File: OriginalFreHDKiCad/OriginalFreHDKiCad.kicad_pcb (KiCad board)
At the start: 2 copper layers, 96.5 x 79 mm, 0 parts

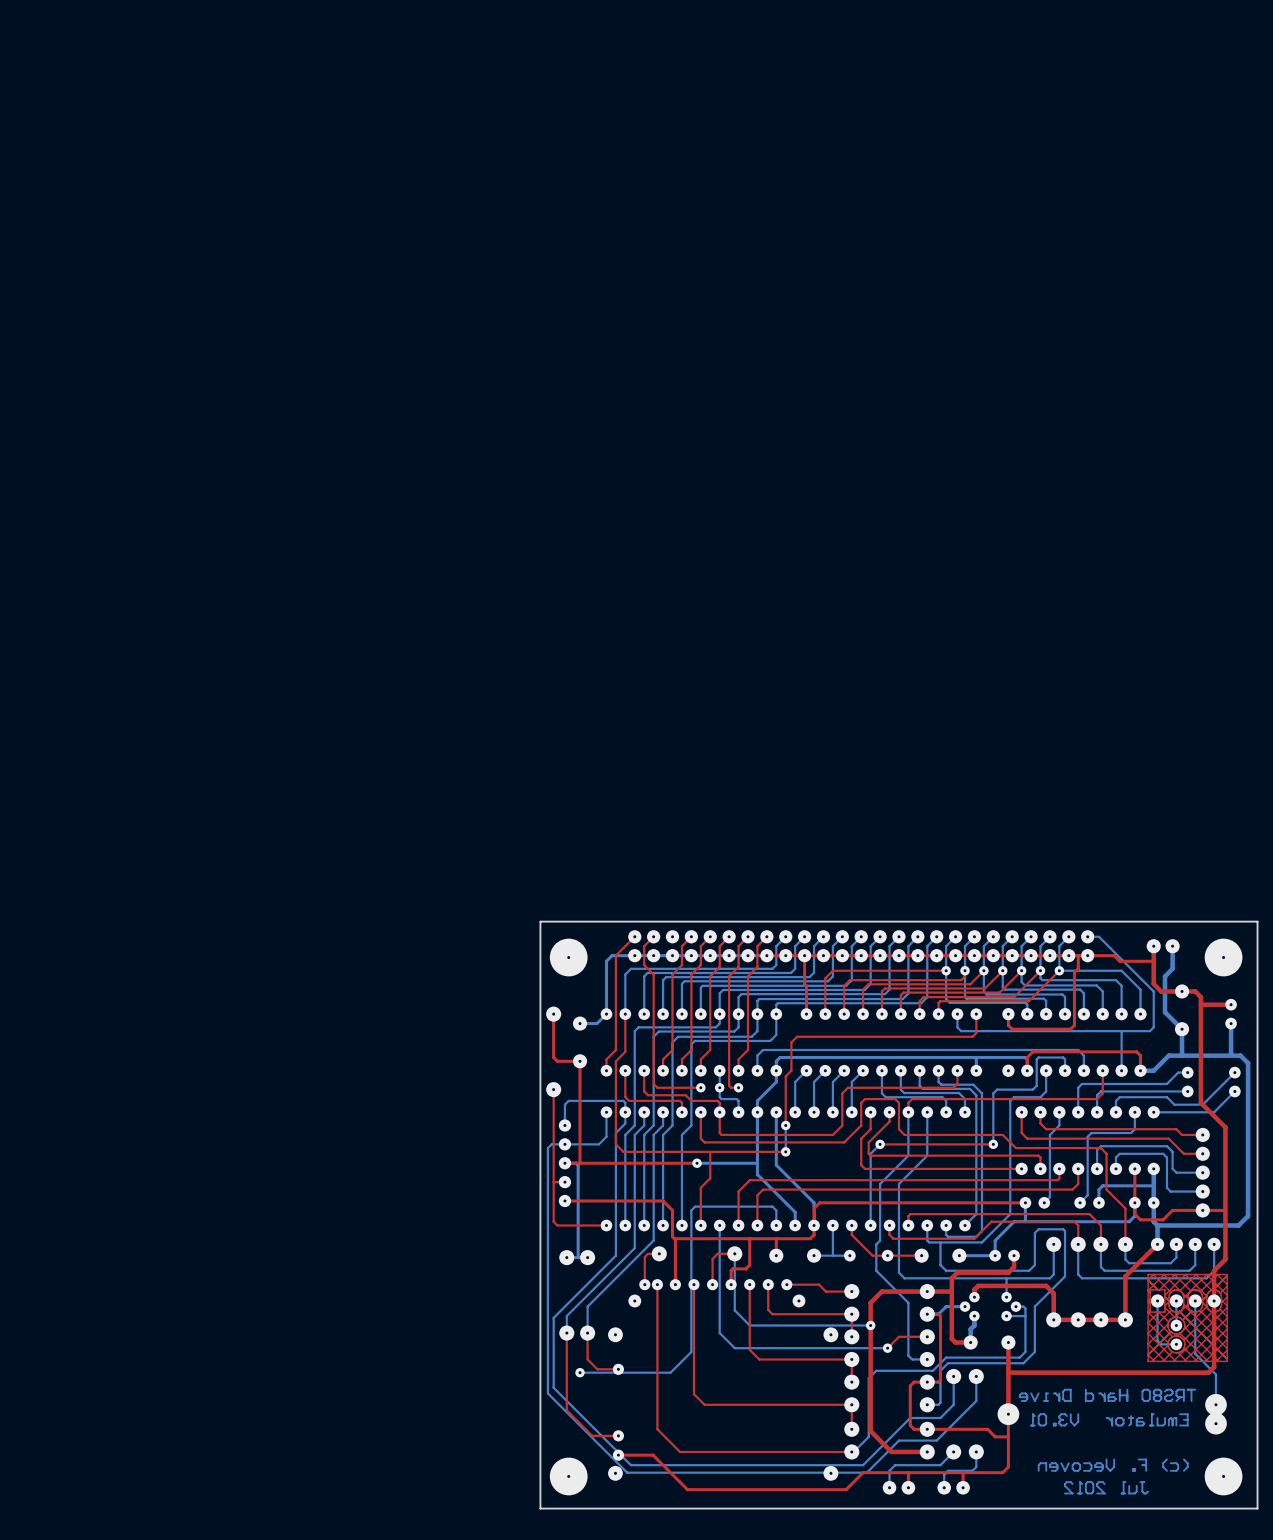
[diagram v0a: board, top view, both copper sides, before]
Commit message: WIP on matching scheamtic to imported gerbers.
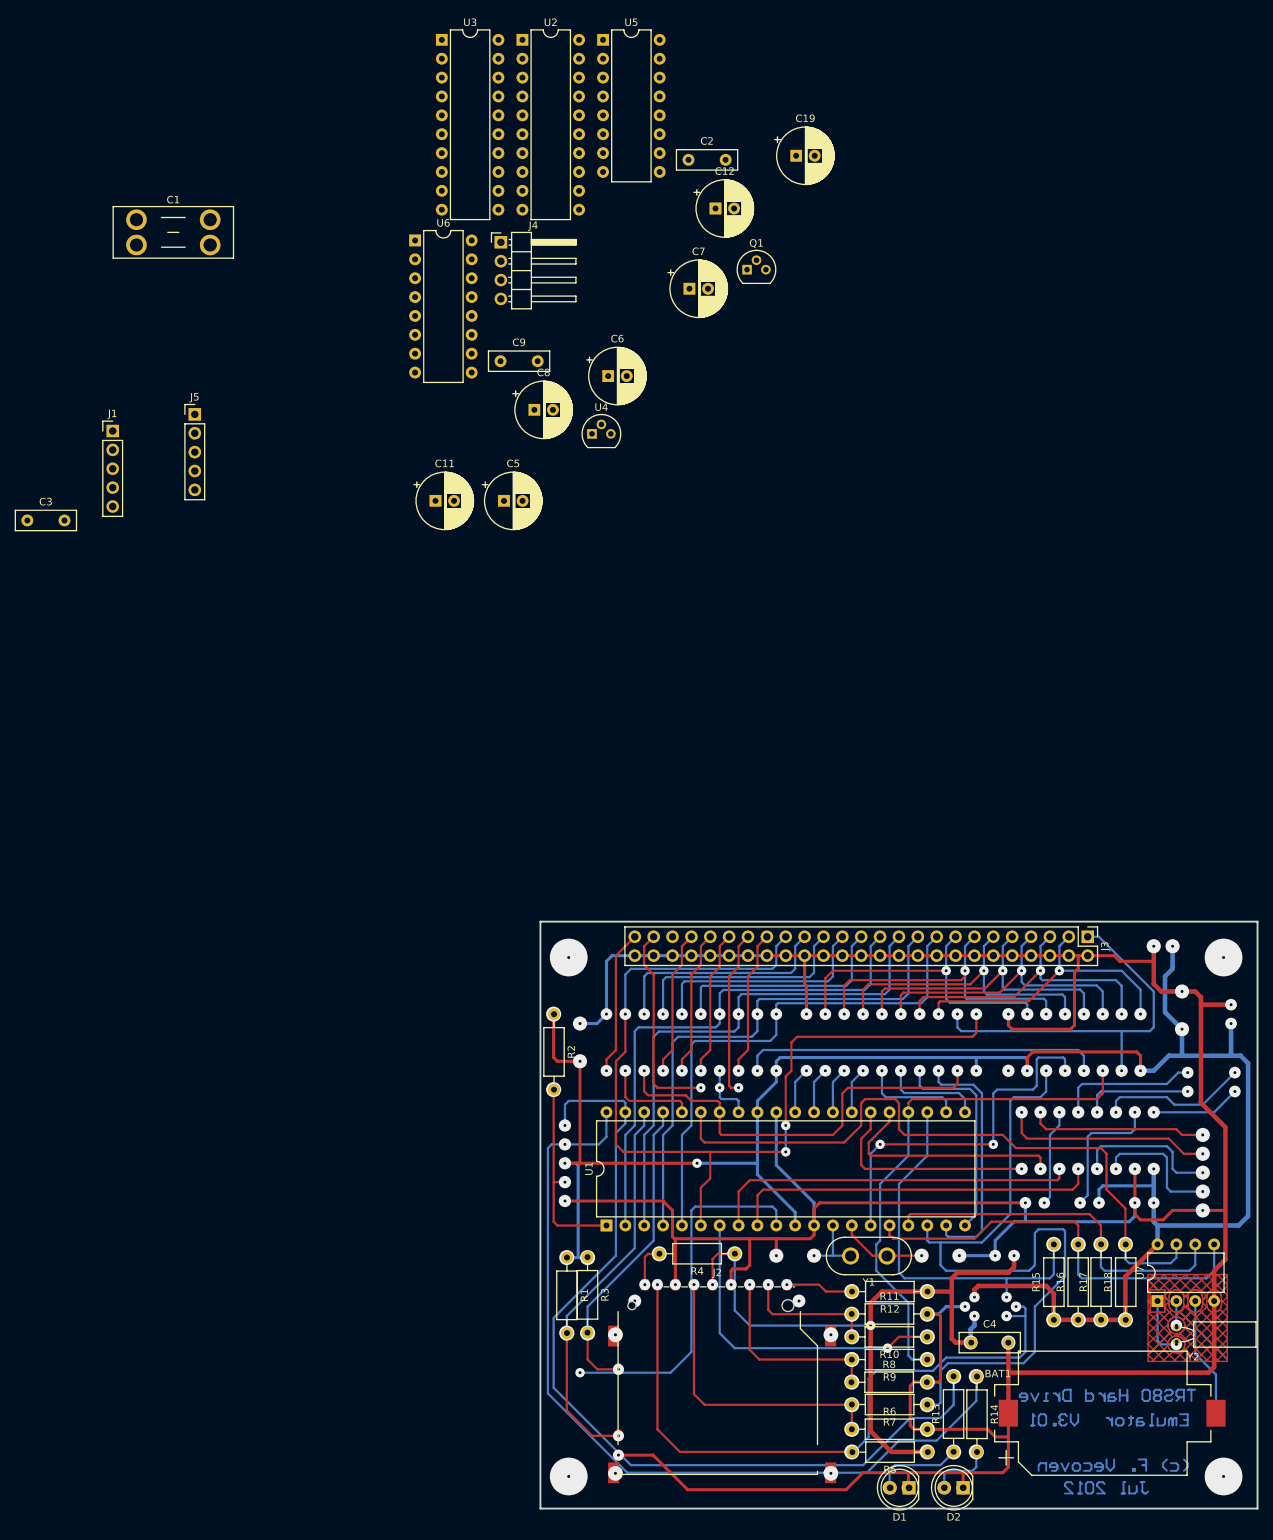
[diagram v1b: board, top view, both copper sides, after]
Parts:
- added BAT1: 3.3V, Battery:BatteryHolder_Keystone_1060_1x2032, F.Cu at (178.7, 123.6)
- added C1: 0.1uF, Fuse:Fuseholder_Blade_Mini_Keystone_3568, F.Cu at (48.6, -37.0)
- added C11: 1uF, Capacitor_THT:CP_Radial_D7.5mm_P2.50mm, F.Cu at (88.9, 0.83)
- added C12: 10uF, Capacitor_THT:CP_Radial_D7.5mm_P2.50mm, F.Cu at (126.6, -38.5)
- added C19: 1uF, Capacitor_THT:CP_Radial_D7.5mm_P2.50mm, F.Cu at (137.4, -45.6)
- added C2: 22pF, Capacitor_THT:C_Disc_D8.0mm_W2.5mm_P5.00mm, F.Cu at (122.9, -45.1)
- added C3: 22pF, Capacitor_THT:C_Disc_D8.0mm_W2.5mm_P5.00mm, F.Cu at (33.9, 3.47)
- added C4: 0.1uF, Capacitor_THT:C_Disc_D8.0mm_W2.5mm_P5.00mm, F.Cu at (161.0, 114.1)
- added C5: 10uF, Capacitor_THT:CP_Radial_D7.5mm_P2.50mm, F.Cu at (98.1, 0.83)
- added C6: 1uF, Capacitor_THT:CP_Radial_D7.5mm_P2.50mm, F.Cu at (112.1, -16.0)
- added C7: 1uF, Capacitor_THT:CP_Radial_D7.5mm_P2.50mm, F.Cu at (123.0, -27.7)
- added C8: 1uF, Capacitor_THT:CP_Radial_D7.5mm_P2.50mm, F.Cu at (102.2, -11.4)
- added C9: 0.1uF, Capacitor_THT:C_Disc_D8.0mm_W2.5mm_P5.00mm, F.Cu at (97.6, -18.0)
- added D1: LED, LED_THT:LED_D5.0mm, F.Cu at (152.6, 133.7)
- added D2: LED, LED_THT:LED_D5.0mm, F.Cu at (159.9, 133.7)
- added J1: CON5, Connector_PinHeader_2.54mm:PinHeader_1x05_P2.54mm_Vertical, F.Cu at (45.4, -8.57)
- added J2: SDCARD, Connector_Card:SD_TE_2041021, F.Cu at (126.8, 118.3)
- added J3: CON50, Connector_PinHeader_2.54mm:PinHeader_2x25_P2.54mm_Vertical, F.Cu at (176.7, 59.5)
- added J4: CON2, Connector_PinHeader_2.54mm:PinHeader_1x04_P2.54mm_Horizontal, F.Cu at (97.7, -34.0)
- added J5: CON5, Connector_PinHeader_2.54mm:PinHeader_1x05_P2.54mm_Vertical, F.Cu at (56.5, -10.8)
- added Q1: BS170, Package_TO_SOT_THT:TO-92, F.Cu at (130.8, -30.3)
- added R1: 1K, Resistor_THT:R_Axial_DIN0207_L6.3mm_D2.5mm_P10.16mm_Horizontal, F.Cu at (106.6, 102.7)
- added R10: 220R, Resistor_THT:R_Axial_DIN0207_L6.3mm_D2.5mm_P10.16mm_Horizontal, F.Cu at (155.0, 113.4)
- added R11: 330R, Resistor_THT:R_Axial_DIN0207_L6.3mm_D2.5mm_P10.16mm_Horizontal, F.Cu at (144.9, 110.3)
- added R12: 10K, Resistor_THT:R_Axial_DIN0207_L6.3mm_D2.5mm_P10.16mm_Horizontal, F.Cu at (155.1, 107.3)
- added R13: 330R, Resistor_THT:R_Axial_DIN0207_L6.3mm_D2.5mm_P10.16mm_Horizontal, F.Cu at (158.6, 128.8)
- added R14: 330R, Resistor_THT:R_Axial_DIN0207_L6.3mm_D2.5mm_P10.16mm_Horizontal, F.Cu at (161.8, 118.7)
- added R15: 10K, Resistor_THT:R_Axial_DIN0207_L6.3mm_D2.5mm_P10.16mm_Horizontal, F.Cu at (172.1, 111.1)
- added R16: 4K7, Resistor_THT:R_Axial_DIN0207_L6.3mm_D2.5mm_P10.16mm_Horizontal, F.Cu at (175.4, 111.1)
- added R17: 4K7, Resistor_THT:R_Axial_DIN0207_L6.3mm_D2.5mm_P10.16mm_Horizontal, F.Cu at (178.4, 111.0)
- added R18: 4K7, Resistor_THT:R_Axial_DIN0207_L6.3mm_D2.5mm_P10.16mm_Horizontal, F.Cu at (181.8, 111.1)
- added R2: 10K, Resistor_THT:R_Axial_DIN0207_L6.3mm_D2.5mm_P10.16mm_Horizontal, F.Cu at (104.8, 69.9)
- added R3: 1K, Resistor_THT:R_Axial_DIN0207_L6.3mm_D2.5mm_P10.16mm_Horizontal, F.Cu at (109.3, 102.6)
- added R4: 10K, Resistor_THT:R_Axial_DIN0207_L6.3mm_D2.5mm_P10.16mm_Horizontal, F.Cu at (129.2, 102.2)
- added R5: 10K, Resistor_THT:R_Axial_DIN0207_L6.3mm_D2.5mm_P10.16mm_Horizontal, F.Cu at (155.1, 128.9)
- added R6: 330R, Resistor_THT:R_Axial_DIN0207_L6.3mm_D2.5mm_P10.16mm_Horizontal, F.Cu at (144.9, 125.8)
- added R7: 220R, Resistor_THT:R_Axial_DIN0207_L6.3mm_D2.5mm_P10.16mm_Horizontal, F.Cu at (155.1, 122.5)
- added R8: 330R, Resistor_THT:R_Axial_DIN0207_L6.3mm_D2.5mm_P10.16mm_Horizontal, F.Cu at (144.8, 119.5)
- added R9: 220R, Resistor_THT:R_Axial_DIN0207_L6.3mm_D2.5mm_P10.16mm_Horizontal, F.Cu at (155.1, 116.4)
- added U1: PIC18F4610, Package_DIP:DIP-40_W15.24mm, F.Cu at (111.9, 98.4)
- added U2: GAL16V8, Package_DIP:DIP-20_W7.62mm, F.Cu at (100.6, -61.2)
- added U3: 74HCT245, Package_DIP:DIP-20_W7.62mm, F.Cu at (89.7, -61.2)
- added U4: LP2950-3.3, Package_TO_SOT_THT:TO-92, F.Cu at (109.9, -8.19)
- added U5: MAX232, Package_DIP:DIP-16_W7.62mm, F.Cu at (111.4, -61.2)
- added U6: 74HC595, Package_DIP:DIP-16_W7.62mm, F.Cu at (86.1, -34.2)
- added U7: DS1307+, Package_DIP:DIP-8_W7.62mm, F.Cu at (186.1, 108.5)
- added Y1: 10MHz, Crystal:Crystal_HC50_Vertical, F.Cu at (149.6, 102.5)
- added Y2: 32.768kHz, Crystal:Crystal_C38-LF_D3.0mm_L8.0mm_Horizontal, F.Cu at (188.6, 114.0)
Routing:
- net (no net): track 4098.3 -> 388.9 mm, vias 299 -> 28
- net GND: track 0.00 -> 903.0 mm, vias 0 -> 32
- net VCC: track 0.00 -> 275.4 mm, vias 0 -> 21
- net ~RD: track 0.00 -> 125.3 mm, vias 0 -> 4
- net Net-(D1-Pad2): track 0.00 -> 118.9 mm, vias 0 -> 2
- net SPI_CLK: track 0.00 -> 101.5 mm, vias 0 -> 2
- net +3V3: track 0.00 -> 96.3 mm, vias 0 -> 8
- net RTC: track 0.00 -> 92.1 mm, vias 0 -> 1
- net Net-(J2-Pad7): track 0.00 -> 90.2 mm, vias 0 -> 4
- net A2: track 0.00 -> 70.3 mm, vias 0 -> 1
- net A0: track 0.00 -> 70.3 mm, vias 0 -> 1
- net A3: track 0.00 -> 70.3 mm, vias 0 -> 1
- net A1: track 0.00 -> 70.2 mm, vias 0 -> 1
- net SPI_SDO: track 0.00 -> 70.1 mm, vias 0 -> 2
- net SDA: track 0.00 -> 57.1 mm, vias 0 -> 1
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
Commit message: Finish matching schematic to imported gerbers - the process found one small error.
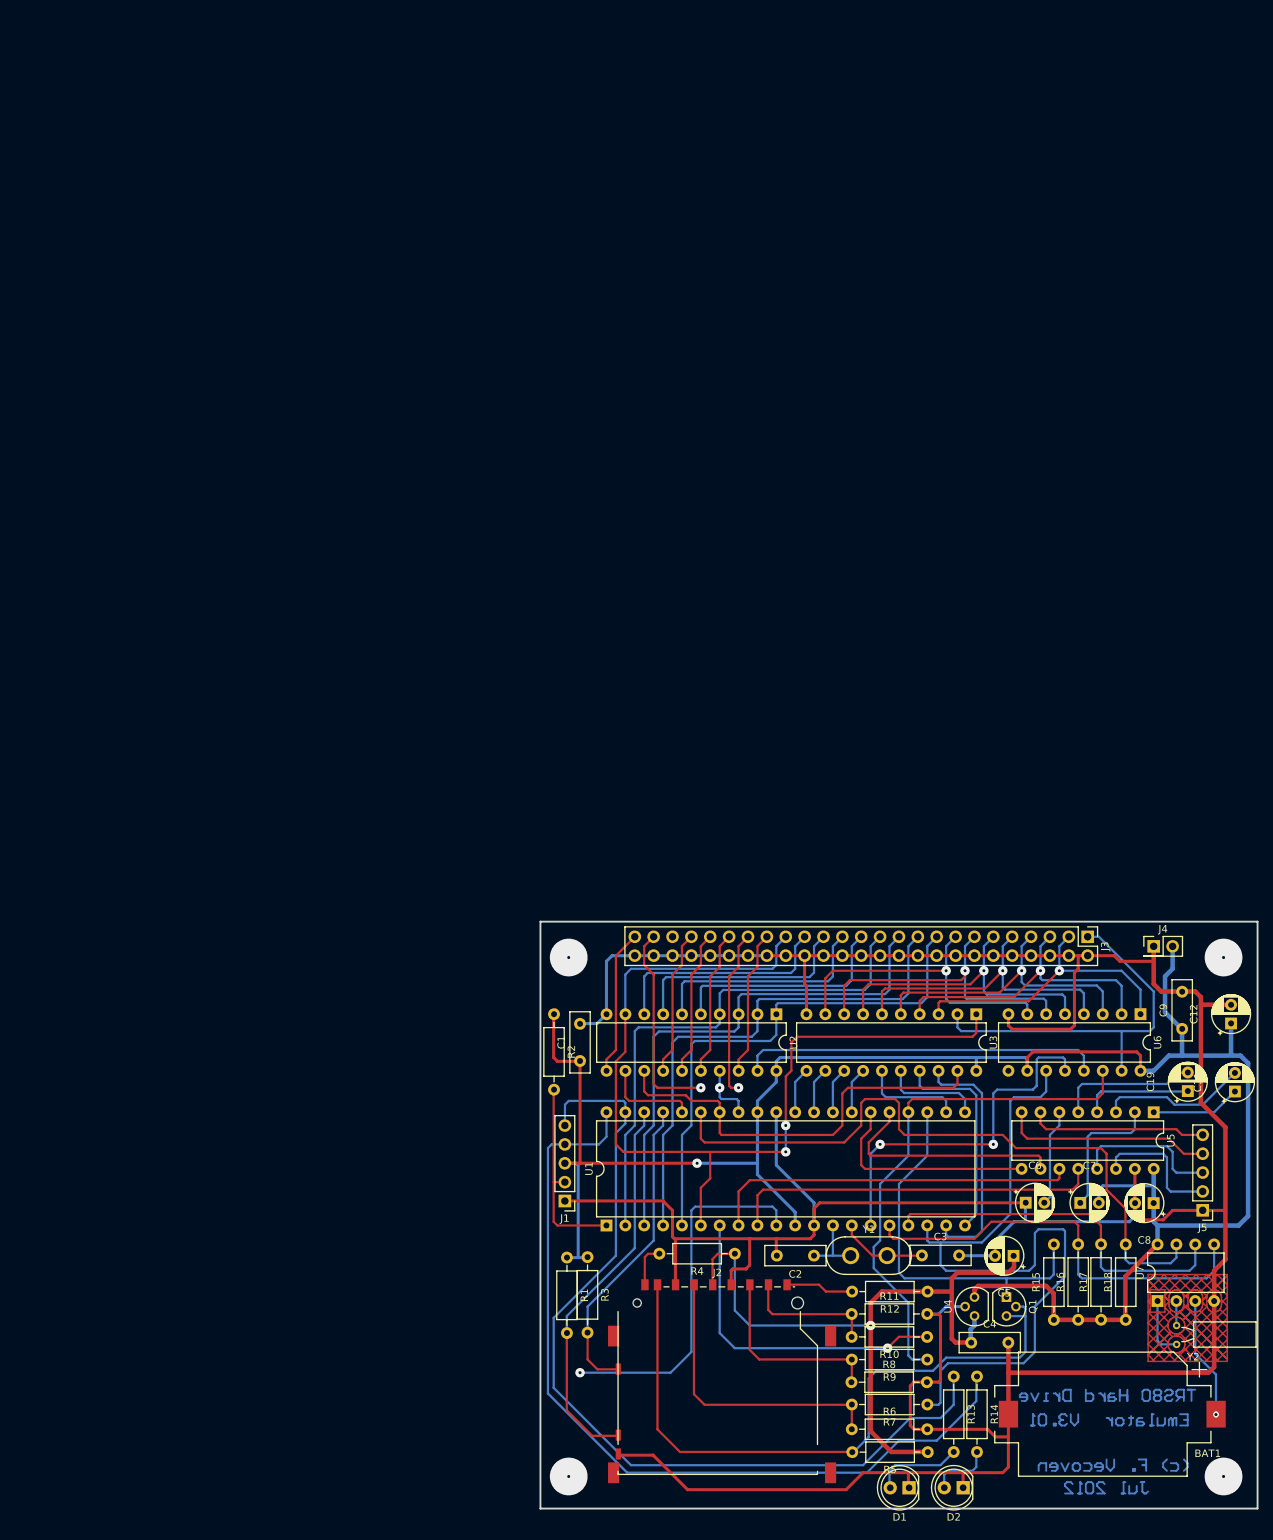
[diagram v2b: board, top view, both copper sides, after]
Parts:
- C1: footprint Fuse:Fuseholder_Blade_Mini_Keystone_3568 -> Capacitor_THT:C_Disc_D8.0mm_W2.5mm_P5.00mm
- C11, C12, C19, C5, C6, C7, C8: footprint Capacitor_THT:CP_Radial_D7.5mm_P2.50mm -> Capacitor_THT:CP_Radial_D5.0mm_P2.50mm
- J4: footprint Connector_PinHeader_2.54mm:PinHeader_1x04_P2.54mm_Horizontal -> Connector_PinHeader_2.54mm:PinHeader_2x01_P2.54mm_Vertical
- moved J5 172.9 mm to (192.1, 96.3), turned to 180 degrees
- moved U5 162.3 mm to (185.5, 83.1), turned to 270 degrees
- moved C3 155.8 mm to (154.3, 102.4)
- moved U3 149.6 mm to (161.7, 69.9), turned to 270 degrees
- moved C2 148.5 mm to (139.8, 102.4), turned to 180 degrees
- moved U6 142.8 mm to (183.8, 69.9), turned to 270 degrees
- moved Q1 142.6 mm to (165.7, 108.0), turned to 270 degrees
- moved C19 136.5 mm to (190.1, 80.3), turned to 90 degrees
- moved U2 135.5 mm to (134.8, 69.9), turned to 270 degrees
- moved C8 135.5 mm to (185.5, 95.3), turned to 180 degrees
- moved C7 133.8 mm to (175.7, 95.3)
- moved C11 133.8 mm to (196.5, 80.3), turned to 90 degrees
- moved C12 129.8 mm to (195.9, 71.2), turned to 90 degrees
- moved U4 129.4 mm to (161.4, 110.5), turned to 90 degrees
- moved J4 129.2 mm to (185.5, 60.8)
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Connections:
- R15 pad 1: +3V3 -> VCC
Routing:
- net (no net): track 388.9 -> 153.3 mm, vias 28 -> 4
- net LED0: track 0.00 -> 114.2 mm
- net GND: track 903.0 -> 788.8 mm, vias 32 -> 0
- net Net-(D1-Pad2): track 118.9 -> 12.0 mm, vias 2 -> 0
- net LED1: track 12.0 -> 118.9 mm, vias 2 -> 0
- net ~STAT_OE: track 0.00 -> 48.6 mm
- net /oRX: track 0.00 -> 28.3 mm
- net /oTX: track 0.00 -> 24.0 mm
- net Net-(C11-Pad2): track 0.00 -> 19.9 mm
- net /oCTS: track 0.00 -> 19.8 mm
- net Net-(C19-Pad2): track 0.00 -> 18.9 mm
- net Net-(C7-Pad1): track 0.00 -> 18.4 mm
- net /oRTS: track 0.00 -> 17.9 mm
- net Net-(C19-Pad1): track 0.00 -> 14.7 mm
- net Net-(C6-Pad2): track 0.00 -> 13.0 mm
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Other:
- net class Default: clearance 0.2 -> 0.05
- rule trace_clearance: 0.2 -> 0.05
